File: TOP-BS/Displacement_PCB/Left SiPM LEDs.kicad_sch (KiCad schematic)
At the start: 36 parts

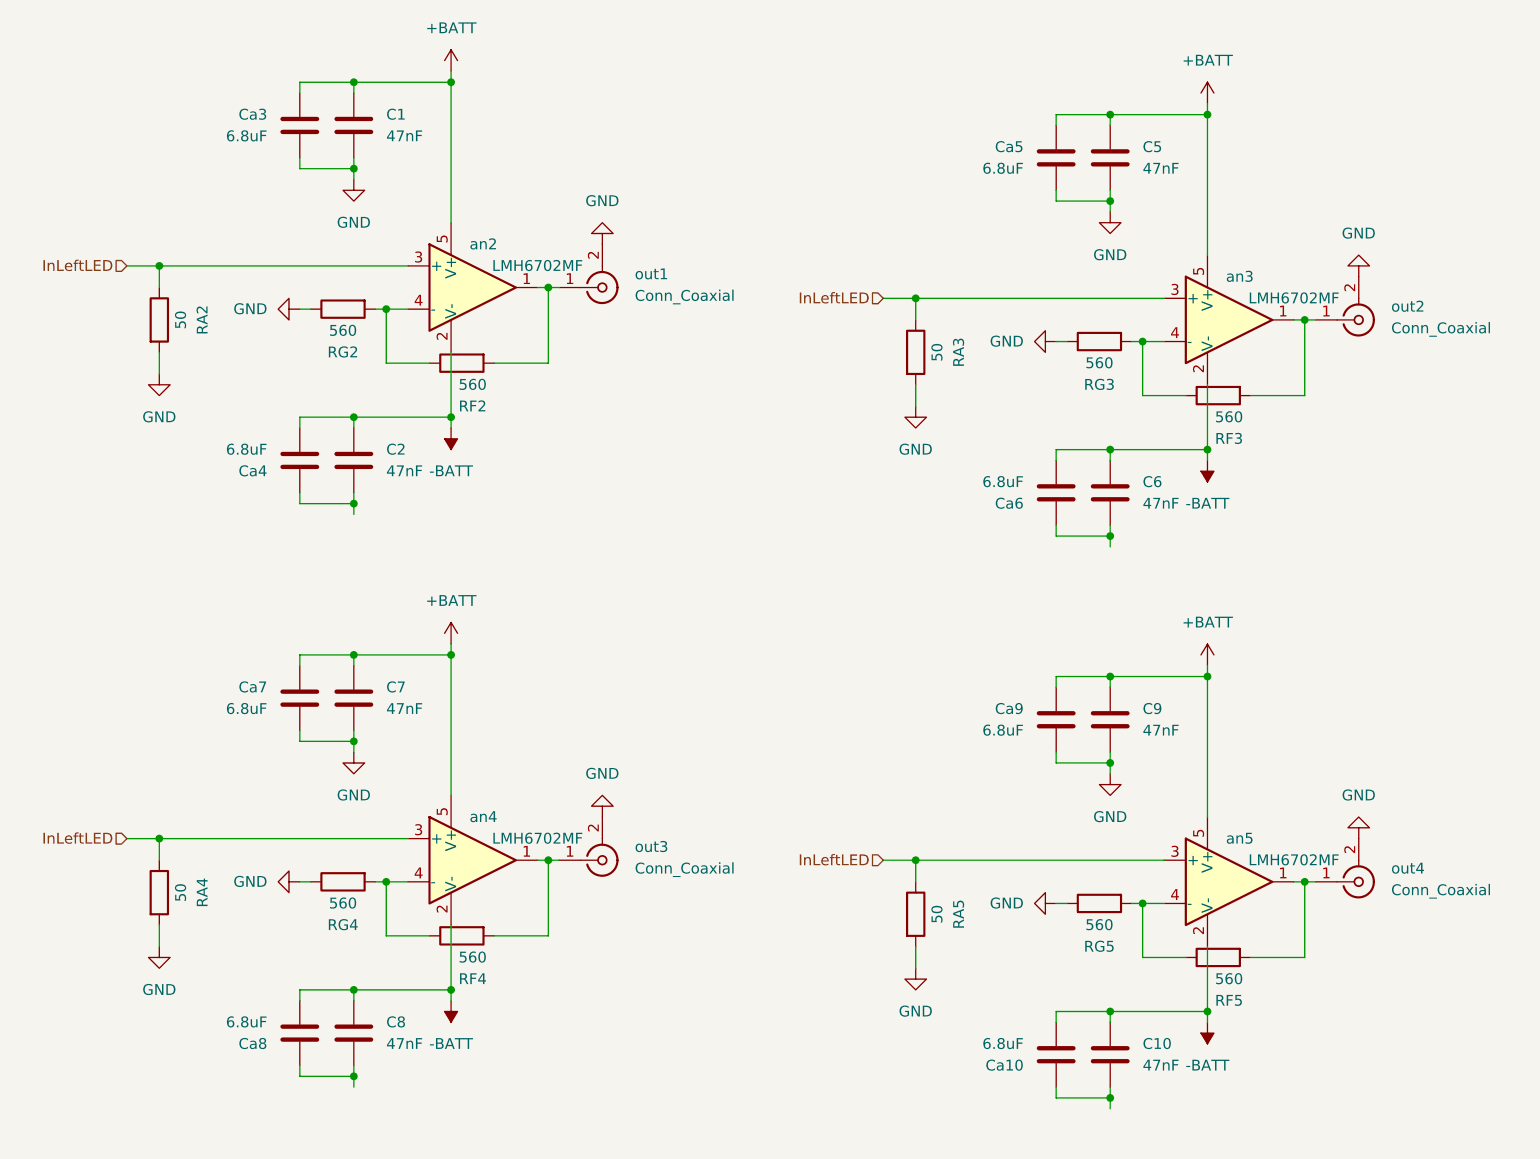
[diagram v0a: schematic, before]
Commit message: Updated Distribution PCB sch
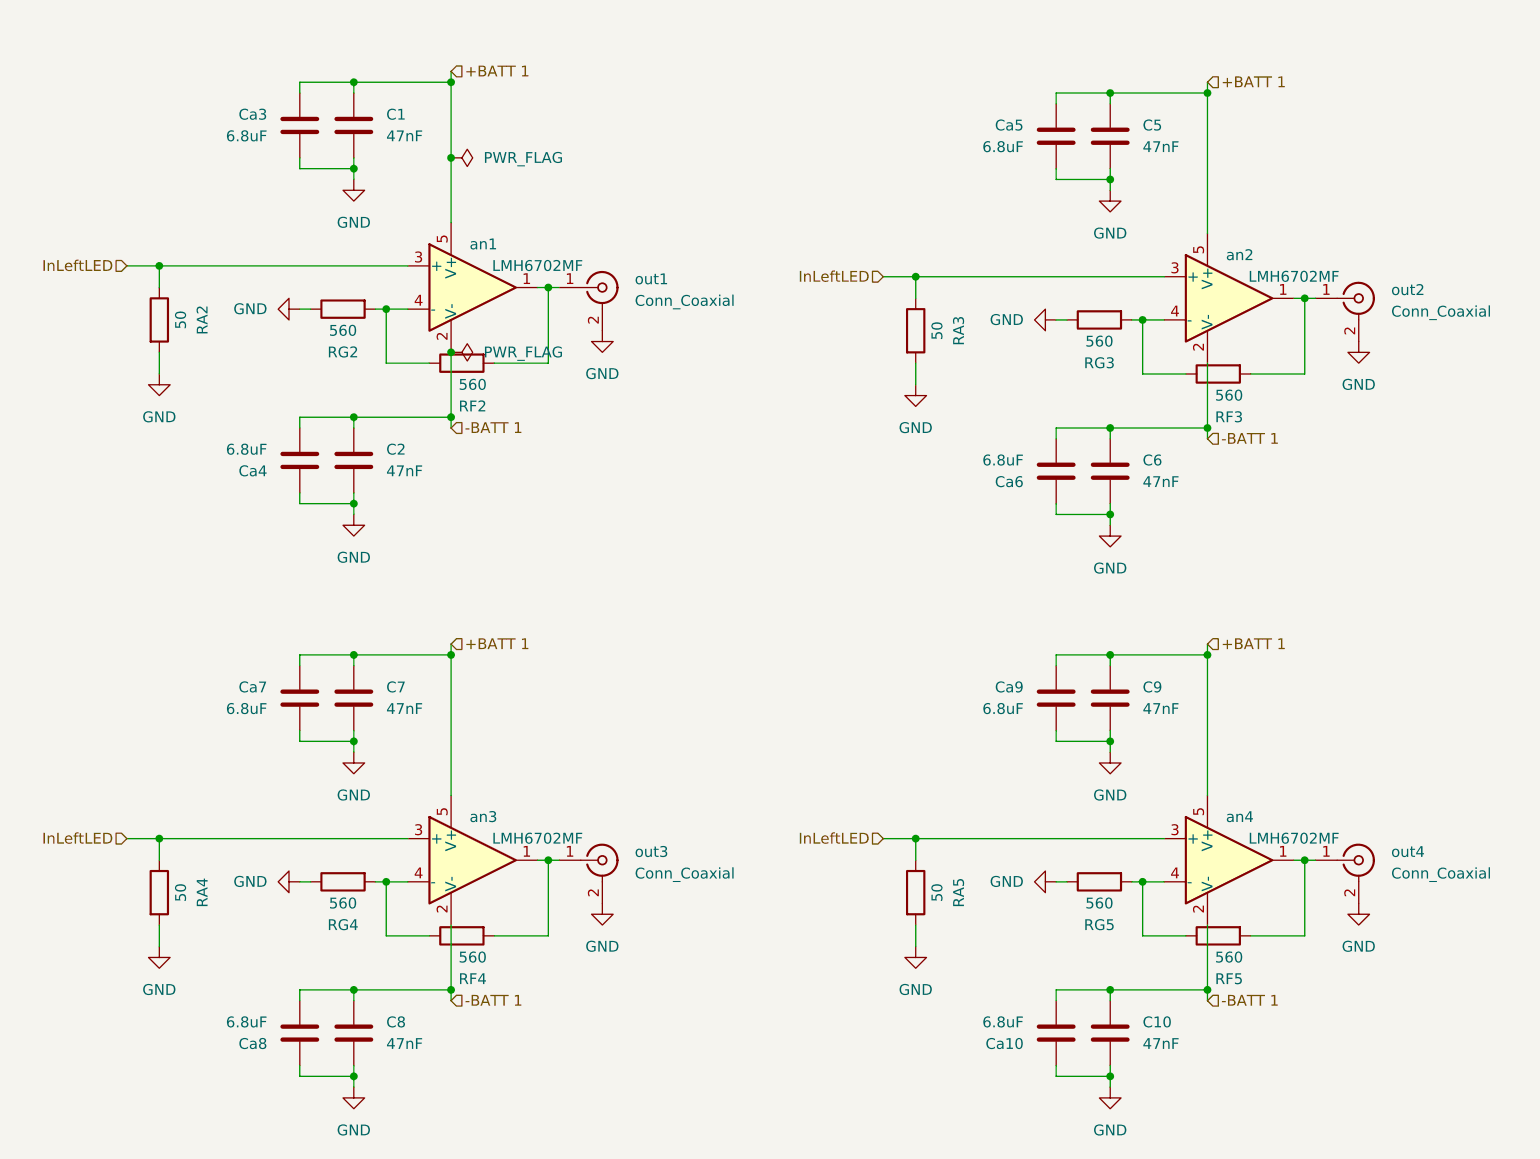
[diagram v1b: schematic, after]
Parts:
- renumbered an2 to an1, an3 to an2, an4 to an3, an5 to an4
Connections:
- net GND: now also C10.2, C2.2, C6.2, C8.2, Ca10.1, Ca4.1, Ca6.1, Ca8.1
- net +BATT renamed +BATT 1
- net -BATT renamed -BATT 1
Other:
- moved on the sheet: C10, C5, C6, C9, Ca10, Ca5, Ca6, Ca9, RA3, RA5, RF3, RF5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
